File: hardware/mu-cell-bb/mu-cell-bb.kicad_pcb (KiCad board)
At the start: 4 copper layers, 65 x 30 mm, 67 parts, among them J1 TX, J2 RX, J3 EXT_CLK, J4 RPi GPIO, J5 IO, U1 24LC256, Y1 32MHz

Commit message: added symbols, worked on PCB
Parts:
- added U2: LDK130M33R, parts:SOT23-5L_1P75X3P05X0P95_STM, F.Cu at (39.3, 61.8)
- OLED1: footprint OLED_128x64:128x64OLED -> parts:OLED_128x64_I2C
- moved OLED1 18.7 mm to (137.4, 113.3)
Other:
- board text added: "RX"
- board text added: "TX"

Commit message: added parts
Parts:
- added JSMA1: TX, parts:BATWIRELESS_BWSMA-KE-P001, F.Cu at (185.6, 103.9)
- added JSMA2: RX, parts:BATWIRELESS_BWSMA-KE-P001, F.Cu at (185.6, 95.7)
- J1, J2: footprint Connector_Coaxial:U.FL_Molex_MCRF_73412-0110_Vertical -> parts:U.FL_Vertical_Passthrough

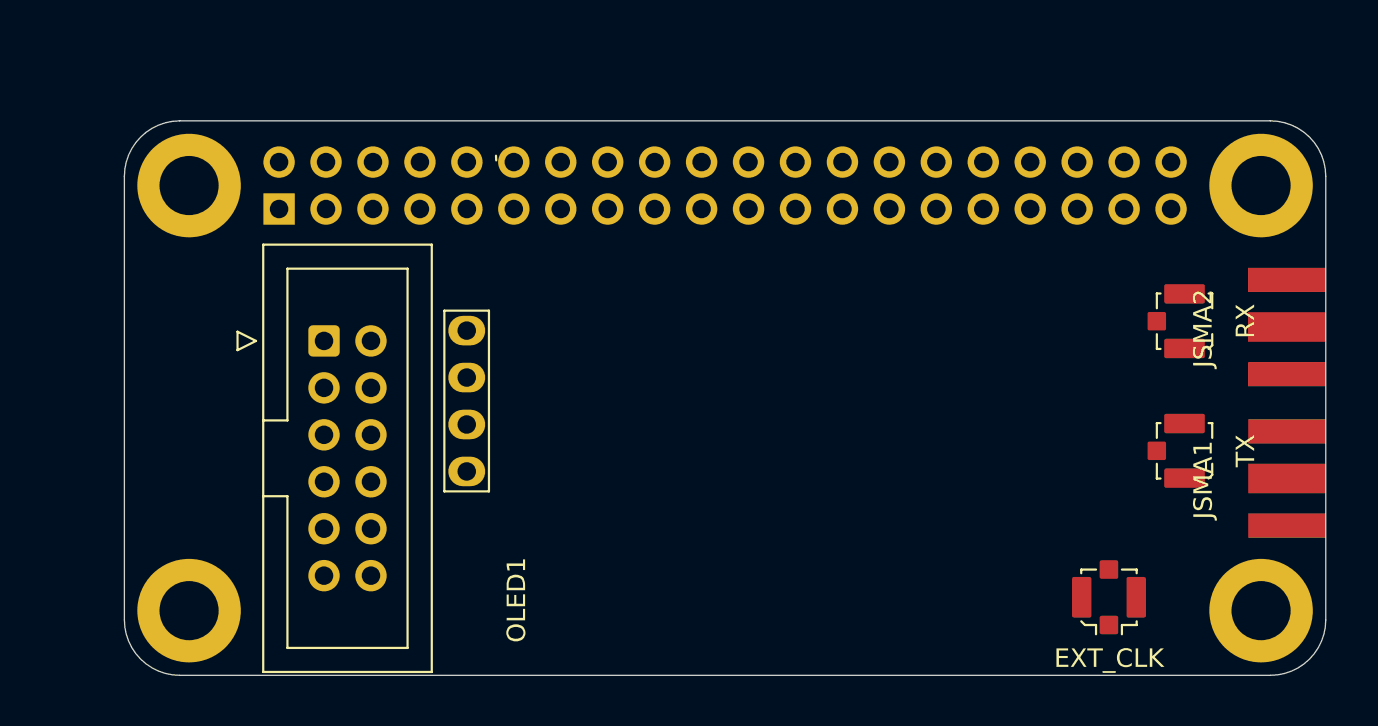
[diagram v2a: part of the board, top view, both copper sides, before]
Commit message: added PCB changes and parts
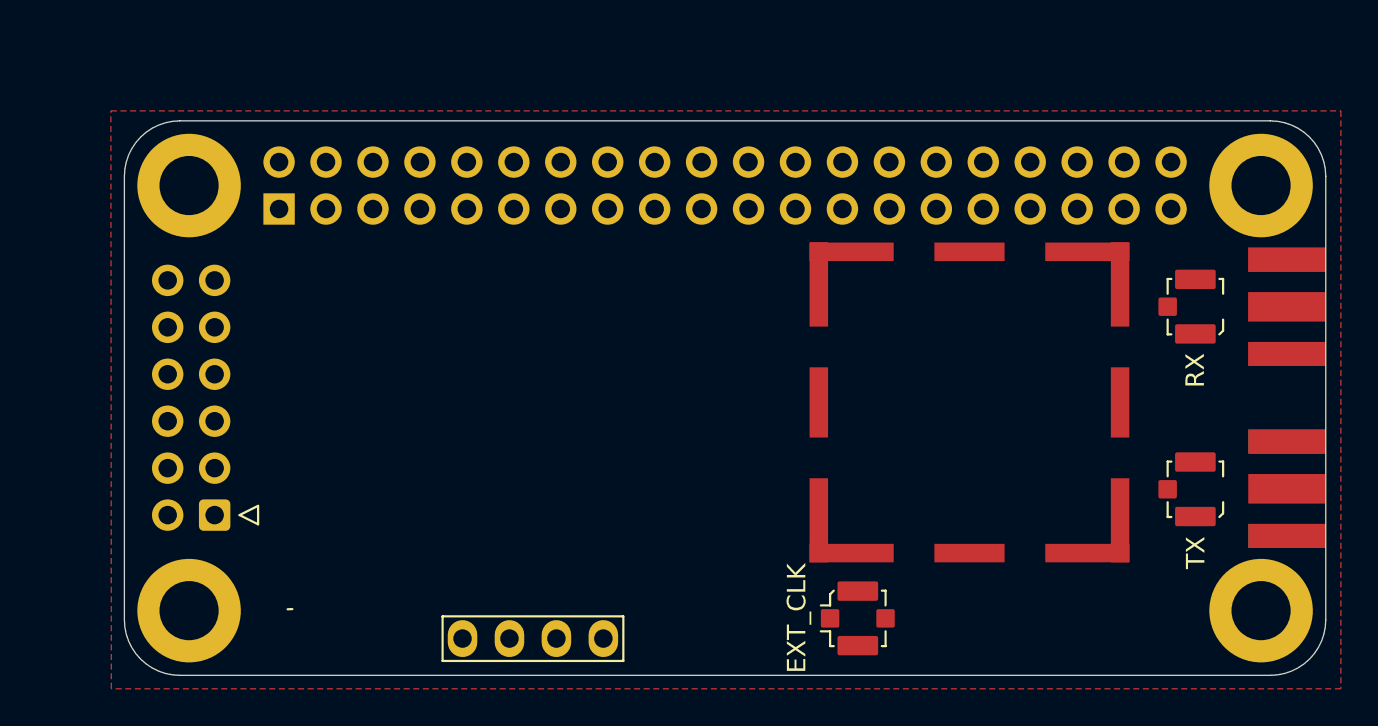
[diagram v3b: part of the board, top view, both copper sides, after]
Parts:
- added RFCAN1: GND, parts:2118707-4 CAN, F.Cu at (157.7, 108.5)
- J5: footprint Connector_IDC:IDC-Header_2x06_P2.54mm_Vertical -> Connector_IDC:IDC-Header_2x06_P2.54mm_Horizontal
- moved OLED1 18.9 mm to (156.3, 114.3), turned to 180 degrees
- moved J3 13.6 mm to (160.3, 111.5), turned to 90 degrees
- moved J5 11.1 mm to (125.5, 105.9), turned to 180 degrees
- moved J1 2.16 mm to (178.5, 104.5)
- moved JSMA2 1.09 mm to (185.6, 94.7)
- moved J2 0.98 mm to (178.5, 94.6)
- moved JSMA1 0.56 mm to (185.6, 104.5)
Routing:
- added copper zone on F.Cu, net GND

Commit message: moved files
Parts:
- added IC1: SX1255IWLTRT, parts:QFN50P500X500X80-33N-D, F.Cu at (166.4, 99.8)
- added Q1: BC817-40W, PCM_Package_TO_SOT_SMD_AKL:SOT-323_SC-70, F.Cu at (43.6, 84.4)
- added Q2: BC817-40W, PCM_Package_TO_SOT_SMD_AKL:SOT-323_SC-70, F.Cu at (43.6, 88.4)
- H1, H2, H3, H4: footprint MountingHole:MountingHole_3.2mm_M3_DIN965_Pad -> PCM_SL_Mechanical:MountingHole_3.2mm_Pad
- J3: footprint Connector_Coaxial:U.FL_Molex_MCRF_73412-0110_Vertical -> parts:U.FL_Vertical_GND
- LED1, LED2, LED3: footprint LED_SMD:LED_0603_1608Metric -> PCM_LED_SMD_AKL:LED_0603_1608Metric
- Y1: footprint Oscillator:Oscillator_SMD_ECS_2520MV-xxx-xx-4Pin_2.5x2.0mm -> parts:Oscillator_SMD_ECS_2520MV-xxx-xx-4Pin_2.5x2.0mm
- moved Y1 125.5 mm to (172.7, 111.5), turned to -90 degrees
- moved JP1 120.1 mm to (165.8, 111.5), turned to 180 degrees
- moved U1 108.1 mm to (153.3, 95.1), turned to 90 degrees
- moved J2 9.69 mm to (178.5, 104.3)
- moved JSMA2 9.69 mm to (185.6, 104.3)
- moved J1 9.67 mm to (178.5, 94.9)
- moved JSMA1 9.67 mm to (185.6, 94.8)

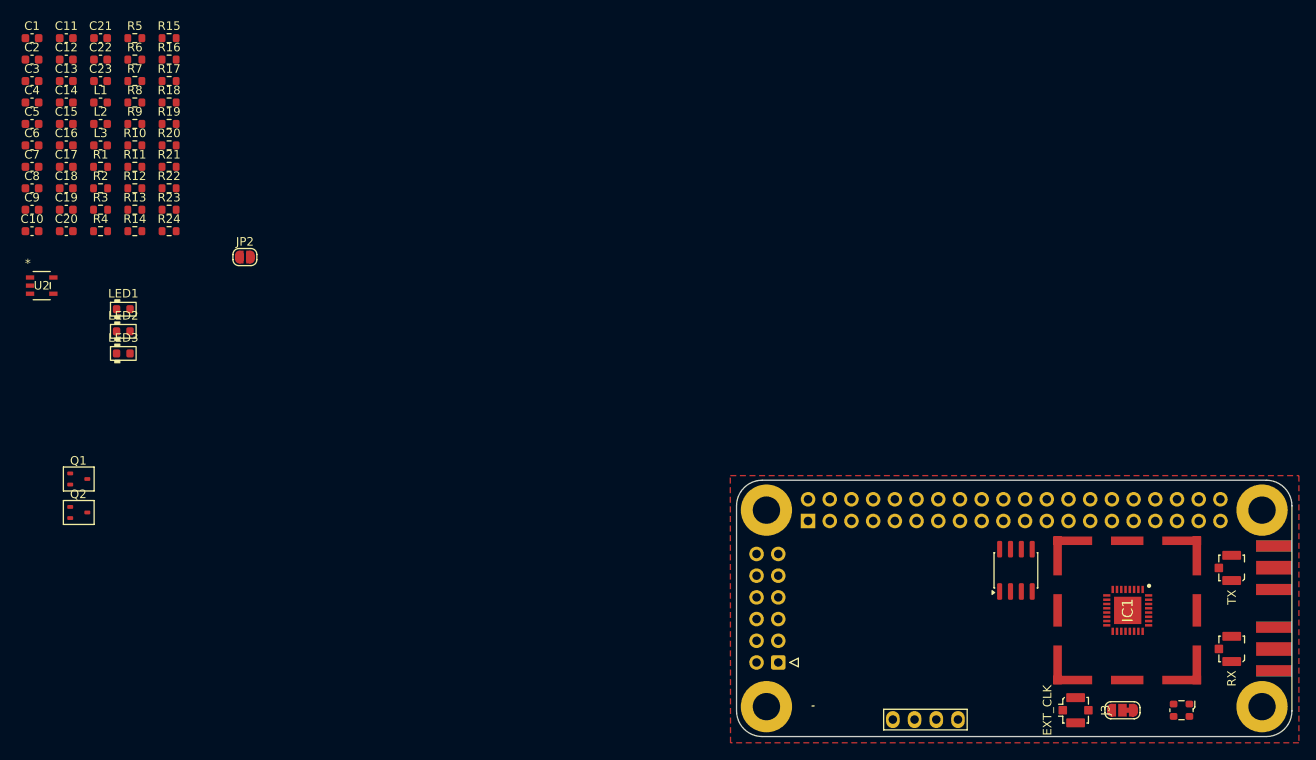
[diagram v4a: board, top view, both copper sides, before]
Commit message: Routed majority of components
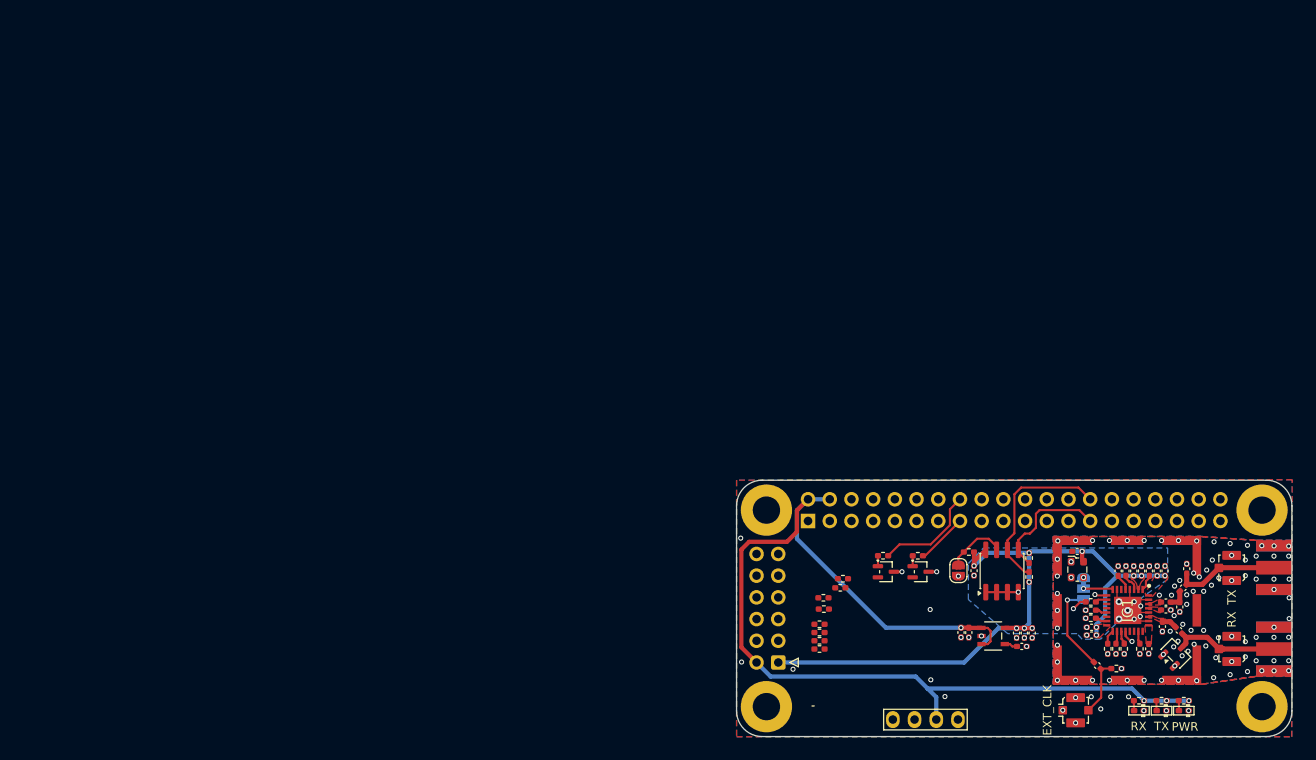
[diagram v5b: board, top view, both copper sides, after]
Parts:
- added D1: BAV99,215, Package_TO_SOT_SMD:SOT-23-3, F.Cu at (172.0, 104.8)
- C1: value 10n -> 33p; footprint Capacitor_SMD:C_0603_1608Metric -> Capacitor_SMD:C_0402_1005Metric_Pad0.74x0.62mm_HandSolder
- C10, C16, C6, C7, C8, C9: footprint Capacitor_SMD:C_0603_1608Metric -> Capacitor_SMD:C_0402_1005Metric_Pad0.74x0.62mm_HandSolder
- C11: value 33p -> 10n; footprint Capacitor_SMD:C_0603_1608Metric -> Capacitor_SMD:C_0402_1005Metric_Pad0.74x0.62mm_HandSolder
- C12: value 27p -> 100n; footprint Capacitor_SMD:C_0603_1608Metric -> Capacitor_SMD:C_0402_1005Metric_Pad0.74x0.62mm_HandSolder
- C13, C17: value 100n -> 10n; footprint Capacitor_SMD:C_0603_1608Metric -> Capacitor_SMD:C_0402_1005Metric_Pad0.74x0.62mm_HandSolder
- C14: value 6.8p -> 100n; footprint Capacitor_SMD:C_0603_1608Metric -> Capacitor_SMD:C_0402_1005Metric_Pad0.74x0.62mm_HandSolder
- C15: value 6.8p -> 10n; footprint Capacitor_SMD:C_0603_1608Metric -> Capacitor_SMD:C_0402_1005Metric_Pad0.74x0.62mm_HandSolder
- C18: value 100n -> 1u; footprint Capacitor_SMD:C_0603_1608Metric -> Capacitor_SMD:C_0402_1005Metric_Pad0.74x0.62mm_HandSolder
- C19: value 1u -> 100n; footprint Capacitor_SMD:C_0603_1608Metric -> Capacitor_SMD:C_0402_1005Metric_Pad0.74x0.62mm_HandSolder
- C2, C3: value 10n -> 6.8p; footprint Capacitor_SMD:C_0603_1608Metric -> Capacitor_SMD:C_0402_1005Metric_Pad0.74x0.62mm_HandSolder
- C20: value 1u -> 10n; footprint Capacitor_SMD:C_0603_1608Metric -> Capacitor_SMD:C_0402_1005Metric_Pad0.74x0.62mm_HandSolder
- C21: value 10n -> 1u; footprint Capacitor_SMD:C_0603_1608Metric -> Capacitor_SMD:C_0402_1005Metric_Pad0.74x0.62mm_HandSolder
- C22: value 4.7u -> 100n; footprint Capacitor_SMD:C_0603_1608Metric -> Capacitor_SMD:C_0402_1005Metric_Pad0.74x0.62mm_HandSolder
- C23: value 100p -> 4.7u; footprint Capacitor_SMD:C_0603_1608Metric -> Capacitor_SMD:C_0402_1005Metric_Pad0.74x0.62mm_HandSolder
- C4: value 10n -> 100p; footprint Capacitor_SMD:C_0603_1608Metric -> Capacitor_SMD:C_0402_1005Metric_Pad0.74x0.62mm_HandSolder
- C5: value 100n -> 27p; footprint Capacitor_SMD:C_0603_1608Metric -> Capacitor_SMD:C_0402_1005Metric_Pad0.74x0.62mm_HandSolder
- JP1: moved to B.Cu
- L1: value 82n -> 33n; footprint Inductor_SMD:L_0603_1608Metric -> Inductor_SMD:L_0402_1005Metric_Pad0.77x0.64mm_HandSolder
- L2: footprint Inductor_SMD:L_0603_1608Metric -> Inductor_SMD:L_0402_1005Metric_Pad0.77x0.64mm_HandSolder
- L3: value 33n -> 82n; footprint Inductor_SMD:L_0603_1608Metric -> Inductor_SMD:L_0402_1005Metric_Pad0.77x0.64mm_HandSolder
- LED1, LED2, LED3: footprint PCM_LED_SMD_AKL:LED_0603_1608Metric -> PCM_LED_SMD_AKL:LED_0402_1005Metric_Pad0.77x0.64mm
- Q1, Q2: footprint PCM_Package_TO_SOT_SMD_AKL:SOT-323_SC-70 -> Package_TO_SOT_SMD:SOT-323_SC-70
- R1, R10, R14, R15, R16, R19, R2, R20, R21, R22, R23, R24, R3, R4, R5, R6, R7, R9: footprint Resistor_SMD:R_0603_1608Metric -> Resistor_SMD:R_0402_1005Metric_Pad0.72x0.64mm_HandSolder
- R11: value 100R -> 3K9; footprint Resistor_SMD:R_0603_1608Metric -> Resistor_SMD:R_0402_1005Metric_Pad0.72x0.64mm_HandSolder
- R12: value 100R -> 1K; footprint Resistor_SMD:R_0603_1608Metric -> Resistor_SMD:R_0402_1005Metric_Pad0.72x0.64mm_HandSolder
- R13: value 1M -> 1K; footprint Resistor_SMD:R_0603_1608Metric -> Resistor_SMD:R_0402_1005Metric_Pad0.72x0.64mm_HandSolder
- R17, R18: value 1K -> 100R; footprint Resistor_SMD:R_0603_1608Metric -> Resistor_SMD:R_0402_1005Metric_Pad0.72x0.64mm_HandSolder
- R8: value 3K9 -> 1M; footprint Resistor_SMD:R_0603_1608Metric -> Resistor_SMD:R_0402_1005Metric_Pad0.72x0.64mm_HandSolder
- moved C2 148.8 mm to (172.5, 99.4), turned to -90 degrees
- moved C1 148.2 mm to (170.8, 98.9)
- moved C3 146.7 mm to (173.3, 94.9), turned to 90 degrees
- moved C5 144.4 mm to (170.8, 99.8)
- moved C6 143.4 mm to (168.8, 104.3), turned to -90 degrees
- moved C4 141.0 mm to (162.8, 106.3), turned to 135 degrees
- moved C11 140.4 mm to (168.0, 95.2), turned to 90 degrees
- moved C14 139.8 mm to (170.7, 95.2), turned to 90 degrees
- moved L2 139.4 mm to (172.4, 102.2), turned to 135 degrees
- moved C7 139.1 mm to (168.9, 95.2), turned to -90 degrees
- moved L1 138.9 mm to (172.9, 97.2), turned to 45 degrees
- moved C15 138.0 mm to (169.8, 95.2), turned to 90 degrees
- moved C12 137.6 mm to (162.1, 102.7), turned to 180 degrees
- moved R15 137.5 mm to (167.7, 110.4), turned to 180 degrees
- moved R12 136.6 mm to (172.9, 110.4), turned to 180 degrees
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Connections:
- net Net-(J2-In) renamed /RF_RX
- C1 pad 1: +3V3 -> /RFO_P
- C1 pad 2: GND -> Net-(C1-Pad2)
- C10 pad 1: GND -> +3V3
- C10 pad 2: Net-(IC1-VR_DIG) -> GND
- C11 pad 1: Net-(IC1-RFO_P) -> +3V3
- C11 pad 2: Net-(C11-Pad2) -> GND
- C12 pad 1: Net-(IC1-RFO_N) -> +3V3
- C13 pad 1: Net-(IC1-VR_ANA2) -> +3V3
- C14 pad 1: Net-(J1-In) -> +3V3
- C15 pad 1: Net-(C11-Pad2) -> +3V3
- C17 pad 1: +5V -> +3V3
- C18 pad 1: +3V3 -> +5V
- C2 pad 1: +3V3 -> Net-(C1-Pad2)
- C20 pad 1: +3V3 -> Net-(U2-BYP/ADJ)
- C21 pad 1: Net-(U2-BYP/ADJ) -> +3V3
- C23 pad 1: Net-(J3-In) -> +3V3
- C23 pad 2: /EXT_CLK -> GND
- C3 pad 1: +3V3 -> /RF_TX
- C4 pad 1: +3V3 -> Net-(J3-In)
- C4 pad 2: GND -> /EXT_CLK
- C5 pad 1: +3V3 -> /RFO_N
- C6 pad 1: +3V3 -> /VR_ANA2
- C7 pad 1: +3V3 -> GND
- C7 pad 2: GND -> /VR_PA
- C8 pad 2: Net-(IC1-VR_PA) -> /VR_ANA1
- C9 pad 2: Net-(IC1-VR_ANAI) -> /VR_DIG
- IC1 pad 1: Net-(IC1-VR_PA) -> /VR_PA
- IC1 pad 25: Net-(IC1-VR_ANA2) -> /VR_ANA2
- IC1 pad 27: Net-(IC1-RFI) -> /RFI
- IC1 pad 29: Net-(IC1-RFO_N) -> /RFO_N
- IC1 pad 3: Net-(IC1-VR_ANAI) -> /VR_ANA1
- IC1 pad 30: Net-(IC1-RFO_P) -> /RFO_P
- IC1 pad 5: Net-(IC1-VR_DIG) -> /VR_DIG
- J1 pad 1: Net-(J1-In) -> /RF_TX
- J4 pad 36: /GPIO17 -> /GPIO16
- JSMA1 pad 1: Net-(J1-In) -> /RF_TX
- L1 pad 1: GND -> Net-(C1-Pad2)
- L1 pad 2: Net-(IC1-RFI) -> /RF_TX
- L2 pad 2: Net-(IC1-RFI) -> /RFI
- L3 pad 1: Net-(C11-Pad2) -> GND
- L3 pad 2: Net-(J1-In) -> /RFI
- R10 pad 2: Net-(JP2-A) -> /ID_SD
- R11 pad 1: /RX_EN -> +3V3
- R11 pad 2: Net-(J5-Pin_3) -> /ID_SC
- R12 pad 1: /TX_EN -> +5V
- R12 pad 2: Net-(J5-Pin_4) -> Net-(LED1-A)
- R13 pad 1: Net-(J3-In) -> +5V
- R13 pad 2: GND -> Net-(LED2-A)
- R14 pad 1: +5V -> Net-(Q1-B)
- R14 pad 2: Net-(LED1-A) -> /TX_EN
- R15 pad 2: Net-(LED2-A) -> Net-(LED3-A)
- R16 pad 1: Net-(Q1-B) -> Net-(Q2-B)
- R16 pad 2: /TX_EN -> /RX_EN
- R17 pad 1: +5V -> /RX_EN
- R17 pad 2: Net-(LED3-A) -> Net-(J5-Pin_3)
- R18 pad 1: Net-(Q2-B) -> /TX_EN
- R18 pad 2: /RX_EN -> Net-(J5-Pin_4)
- R19 pad 1: /GPIO04 -> /RXD
- R19 pad 2: Net-(J5-Pin_9) -> Net-(J5-Pin_5)
- R20 pad 1: /RXD -> /TXD
- R20 pad 2: Net-(J5-Pin_5) -> Net-(J5-Pin_6)
- R22 pad 1: /TXD -> /SCL
- R22 pad 2: Net-(J5-Pin_6) -> Net-(J5-Pin_8)
- R23 pad 1: /SCL -> /GPIO04
- R23 pad 2: Net-(J5-Pin_8) -> Net-(J5-Pin_9)
- R4 pad 1: /DIO2 -> /SCK
- R4 pad 2: Net-(IC1-DIO2) -> Net-(IC1-SCK)
- R5 pad 1: /MOSI -> /MISO
- R5 pad 2: Net-(IC1-MOSI) -> Net-(IC1-MISO)
- R6 pad 1: /MISO -> /MOSI
- R6 pad 2: Net-(IC1-MISO) -> Net-(IC1-MOSI)
- R7 pad 1: /SCK -> /DIO2
- R7 pad 2: Net-(IC1-SCK) -> Net-(IC1-DIO2)
- R8 pad 1: +3V3 -> Net-(J3-In)
- R8 pad 2: /ID_SC -> GND
- R9 pad 2: /ID_SD -> Net-(JP2-A)
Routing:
- net +5V: track 0.00 -> 119.4 mm, vias 0 -> 4
- net +3V3: track 0.00 -> 80.3 mm, vias 0 -> 13
- net Net-(LED2-K): track 0.00 -> 38.4 mm, vias 0 -> 2
- net Net-(LED3-K): track 0.00 -> 37.9 mm, vias 0 -> 2
- net /CK_OUT: track 0.00 -> 31.8 mm, vias 0 -> 1
- net /~{CS}: track 0.00 -> 28.9 mm, vias 0 -> 1
- net /I_IN: track 0.00 -> 28.2 mm, vias 0 -> 1
- net /MOSI: track 0.00 -> 27.8 mm, vias 0 -> 1
- net /MISO: track 0.00 -> 24.1 mm, vias 0 -> 1
- net /DIO2: track 0.00 -> 24.0 mm, vias 0 -> 1
- net /I_OUT: track 0.00 -> 23.3 mm, vias 0 -> 1
- net /SCK: track 0.00 -> 21.1 mm, vias 0 -> 1
- net /ID_SC: track 0.00 -> 20.6 mm
- net GND: track 0.00 -> 17.8 mm, vias 0 -> 138
- net /ID_SD: track 0.00 -> 14.6 mm
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- added copper zone on B.Cu, net +3V3
- added copper zone on F.Cu, net +3V3
- added copper zone on F.Cu, net /RFI
- added copper zone on F.Cu, net /RFO_N
- added copper zone on F.Cu, net /RFO_P
- added copper zone on F.Cu, net /VR_ANA2
- added copper zone on B.Cu, net GND
- added copper zone on In2.Cu, net GND
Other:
- board text added: "PWR"

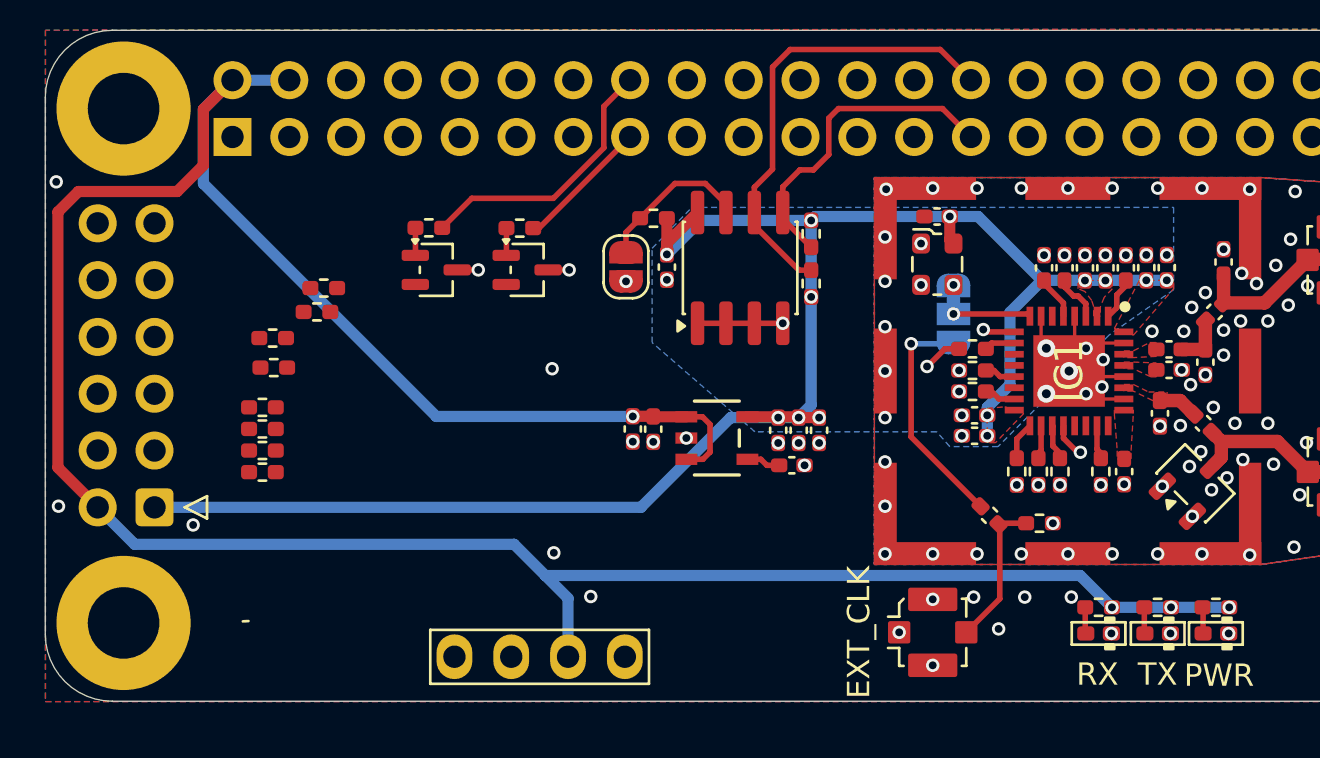
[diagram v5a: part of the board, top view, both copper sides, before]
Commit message: added LCSC parts, finished routing
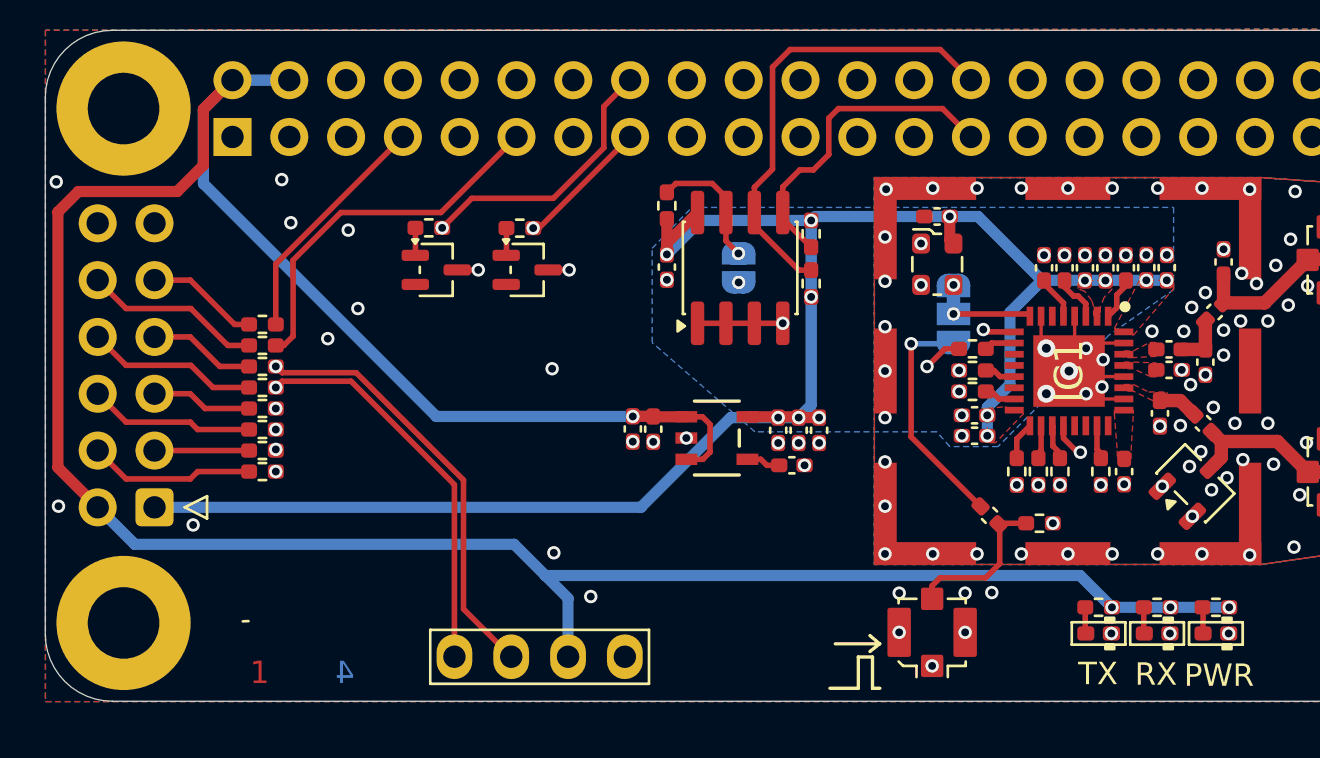
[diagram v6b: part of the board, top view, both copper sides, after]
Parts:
- added REF**: LayerMarker_4_6.35x2.54mm_TextH1mm_P1.27mm_LowerMirrored, Symbol:LayerMarker_4_6.35x2.54mm_TextH1mm_P1.27mm_LowerMirrored, F.Cu at (130.2, 114.6)
- JP2: moved to B.Cu
- LED1: value LED_0603 -> Green
- LED2: value LED_0603 -> Red
- LED3: value LED_0603 -> Yellow
- moved JP2 5.04 mm to (151.6, 95.2)
- moved R24 3.76 mm to (130.3, 98.7), turned to 180 degrees
- moved LED2 2.64 mm to (167.7, 111.6)
- moved R13 2.64 mm to (167.7, 110.4)
- moved LED3 2.62 mm to (170.3, 111.6)
- moved R15 2.62 mm to (170.3, 110.4)
- moved R23 2.50 mm to (130.3, 97.7)
- moved R22 2.26 mm to (130.3, 100.6)
- moved R20 0.99 mm to (130.3, 102.4)
- moved R19 0.91 mm to (130.3, 101.5)
- moved R9 0.82 mm to (148.4, 92.4), turned to 90 degrees
- moved R21 0.51 mm to (130.3, 99.6)
- turned J3 to 180 degrees
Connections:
- R19 pad 1: /RXD -> /TXD
- R20 pad 1: /TXD -> /RXD
- R21 pad 1: /SDA -> /SCL
- R22 pad 1: /SCL -> /SDA
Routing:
- net /SCL: track 0.00 -> 30.8 mm, vias 0 -> 1
- net /SDA: track 0.00 -> 29.7 mm, vias 0 -> 1
- net /RXD: track 0.00 -> 19.0 mm, vias 0 -> 1
- net /TXD: track 0.00 -> 17.2 mm, vias 0 -> 1
- net /TX_EN: track 6.02 -> 22.9 mm, vias 0 -> 2
- net /GPIO17: track 0.00 -> 16.6 mm
- net /RX_EN: track 12.2 -> 25.4 mm, vias 0 -> 2
- net /GPIO04: track 0.00 -> 10.7 mm
- net Net-(J5-Pin_10): track 0.00 -> 7.98 mm
- net Net-(J5-Pin_8): track 0.00 -> 7.70 mm
- net Net-(J5-Pin_6): track 0.00 -> 7.43 mm
- net Net-(J5-Pin_4): track 0.00 -> 7.43 mm
- net Net-(LED3-K): track 37.9 -> 44.7 mm
- net Net-(J5-Pin_9): track 0.00 -> 5.05 mm
- net Net-(J5-Pin_7): track 0.00 -> 4.78 mm
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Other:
- board text removed: "EXT_CLK"
